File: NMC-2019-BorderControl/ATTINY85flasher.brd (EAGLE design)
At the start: 52.5 x 52.5 mm, 16 parts, among them J1 ICSP-LO-SILK

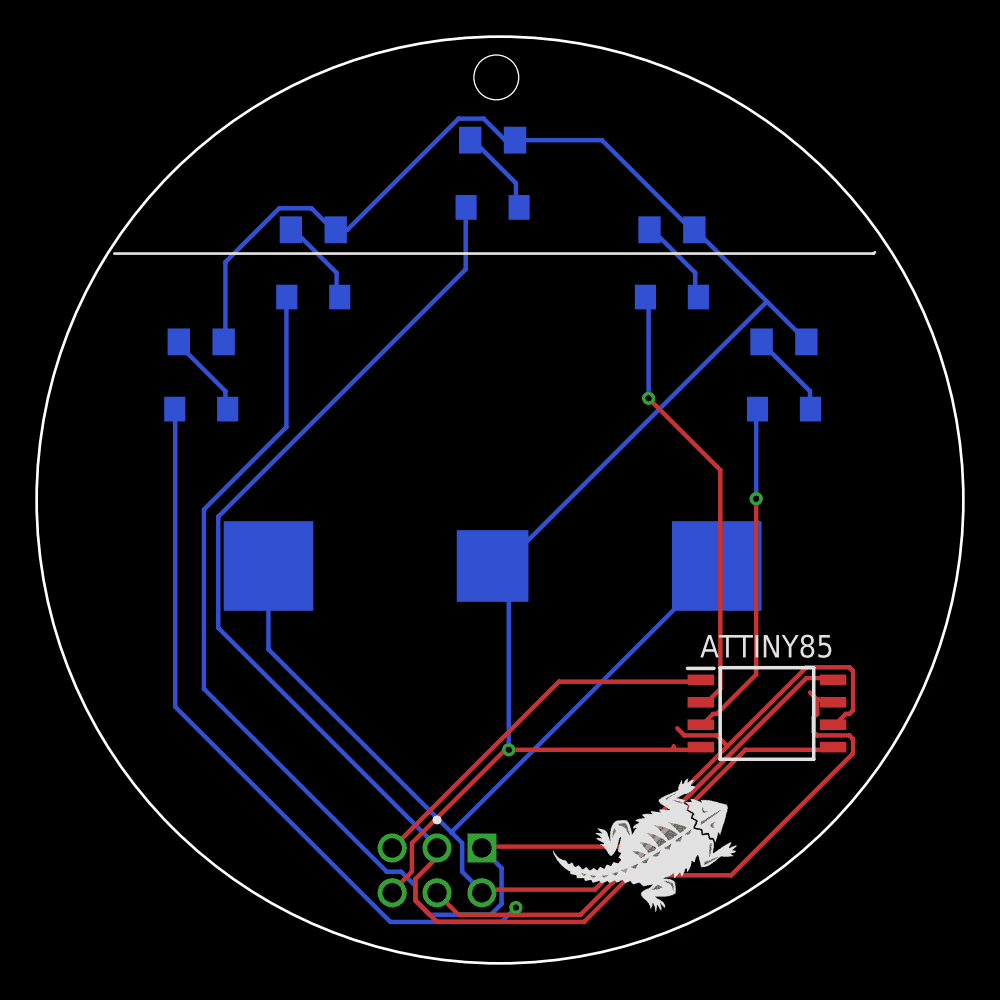
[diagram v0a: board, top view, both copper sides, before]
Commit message: corrected polarity
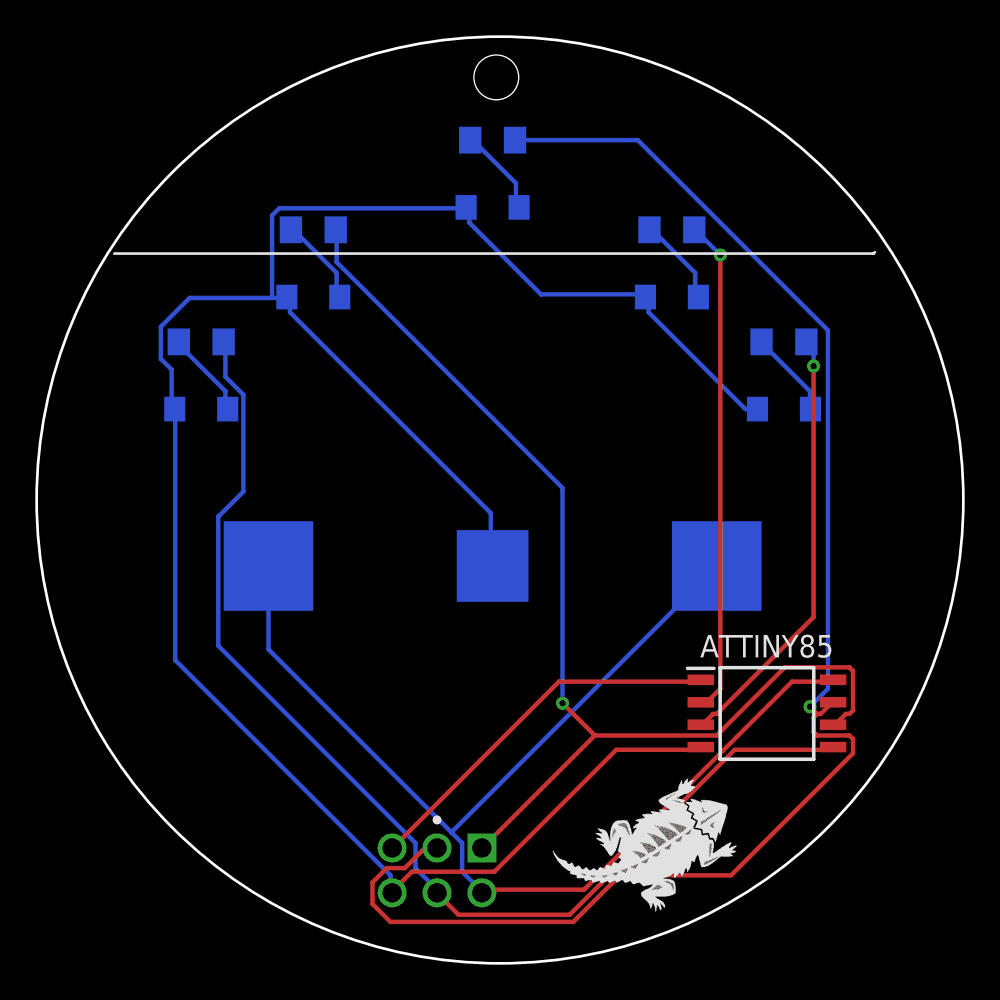
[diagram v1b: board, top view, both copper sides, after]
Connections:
- net GND: now also D1.C, D2.C, D3.C, D4.C, D5.C; no longer R1.1, R2.1, R3.1, R4.1, R5.1
- net OUT0: now also R1.1; no longer D1.C
- net OUT1: now also R2.1; no longer D2.C
- net OUT2: now also R3.1; no longer D3.C
- net OUT3: now also R4.1; no longer D4.C
- net OUT4: now also R5.1; no longer D5.C
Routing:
- net GND: track 102.8 -> 124.6 mm, vias 1 -> 0
- net OUT1: track 83.0 -> 63.8 mm, vias 0 -> 1
- net OUT4: track 19.4 -> 24.7 mm
- net OUT0: track 68.9 -> 64.3 mm, vias 1 -> 0
- net OUT3: track 25.5 -> 28.1 mm
- net OUT2: track 86.7 -> 87.4 mm, vias 0 -> 1
